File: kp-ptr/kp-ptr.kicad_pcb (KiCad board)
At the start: 4 copper layers, 31.6 x 104.6 mm, 169 parts, among them IC1 E22-900M22S, J1 ESP32_PROG_CON, J10 Conn_01x02, J11 Conn_01x02, J12 Conn_01x02, J13 Conn_01x02, J2 Conn_01x02, J3 Conn_01x02, J4 USB_C_Receptacle_USB2.0, J5 u.fl, J6 Conn_01x06_Male, J7 Conn_01x10_Male, J8 Conn_01x06_Male, J9 Conn_01x02_Male, Q1 NMOS_SOT23, Q2 DMC2025UFDB_v2, Q3 DMC2025UFDB_v2, Q4 DMC2025UFDB_v2, Q5 DMC2025UFDB_v2, U1 ESP32-S3FN8, U10 W25Q128JVS, U11 NL27WZU04DBVT1G, U2 MS560702BA03-50, U3 MMC5983MA, U4 H3LIS331, U5 L76-L, U6 NJG1156PCD, U7 LSM6DSO32, U9 USBLC6-2SC6, Y1 7M40000005-40MHz

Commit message: swiatelko w tunelu aby zmiescic wszystko
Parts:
- IC1, J4, J6, J7, J8, LS1, U5: moved to B.Cu
- J10, J12, J3: footprint TerminalBlock_Phoenix:TerminalBlock_Phoenix_MPT-0,5-2-2.54_1x02_P2.54mm_Horizontal -> TerminalBlock_TE-Connectivity:TerminalBlock_TE_282834-2_1x02_P2.54mm_Horizontal; moved to B.Cu
- J11, J13: footprint TerminalBlock_Phoenix:TerminalBlock_Phoenix_MPT-0,5-2-2.54_1x02_P2.54mm_Horizontal -> TerminalBlock_TE-Connectivity:TerminalBlock_TE_282834-2_1x02_P2.54mm_Horizontal
- J2: footprint Connector_JST:JST_GH_SM02B-GHS-TB_1x02-1MP_P1.25mm_Horizontal -> TerminalBlock_TE-Connectivity:TerminalBlock_TE_282834-2_1x02_P2.54mm_Horizontal; moved to B.Cu
- J9: footprint Connector_JST:JST_GH_BM02B-GHS-TBT_1x02-1MP_P1.25mm_Vertical -> TerminalBlock_TE-Connectivity:TerminalBlock_TE_282834-2_1x02_P2.54mm_Horizontal; moved to B.Cu
- moved C20 172.2 mm to (165.3, 49.3)
- moved C21 172.2 mm to (165.3, 48.3)
- moved R15 172.2 mm to (170.3, 47.3)
- moved U4 172.2 mm to (167.8, 48.8)
- moved C22 172.2 mm to (165.3, 50.3)
- moved C28 163.4 mm to (146.4, 37.3)
- moved C29 163.4 mm to (147.1, 37.3)
- moved C31 163.4 mm to (147.8, 37.3)
- moved R18 163.4 mm to (152.0, 39.3)
- moved U7 163.4 mm to (149.8, 38.2)
- moved R30 46.1 mm to (157.6, 40.8), turned to 0 degrees
- moved C39 28.7 mm to (163.6, 57.7)
- moved R26 28.7 mm to (165.6, 53.0)
- moved R27 28.7 mm to (172.0, 56.5)
- moved C40 28.7 mm to (162.6, 57.7)
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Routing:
- net VBUS: track 9.83 -> 0.00 mm
- net Net-(J4-PadA7): track 2.94 -> 0.00 mm
- net Net-(J4-PadA6): track 2.85 -> 0.00 mm
- net (no net): vias 0 -> 4
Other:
- board size 31.6 x 104.6 mm -> 31.6 x 101.5 mm

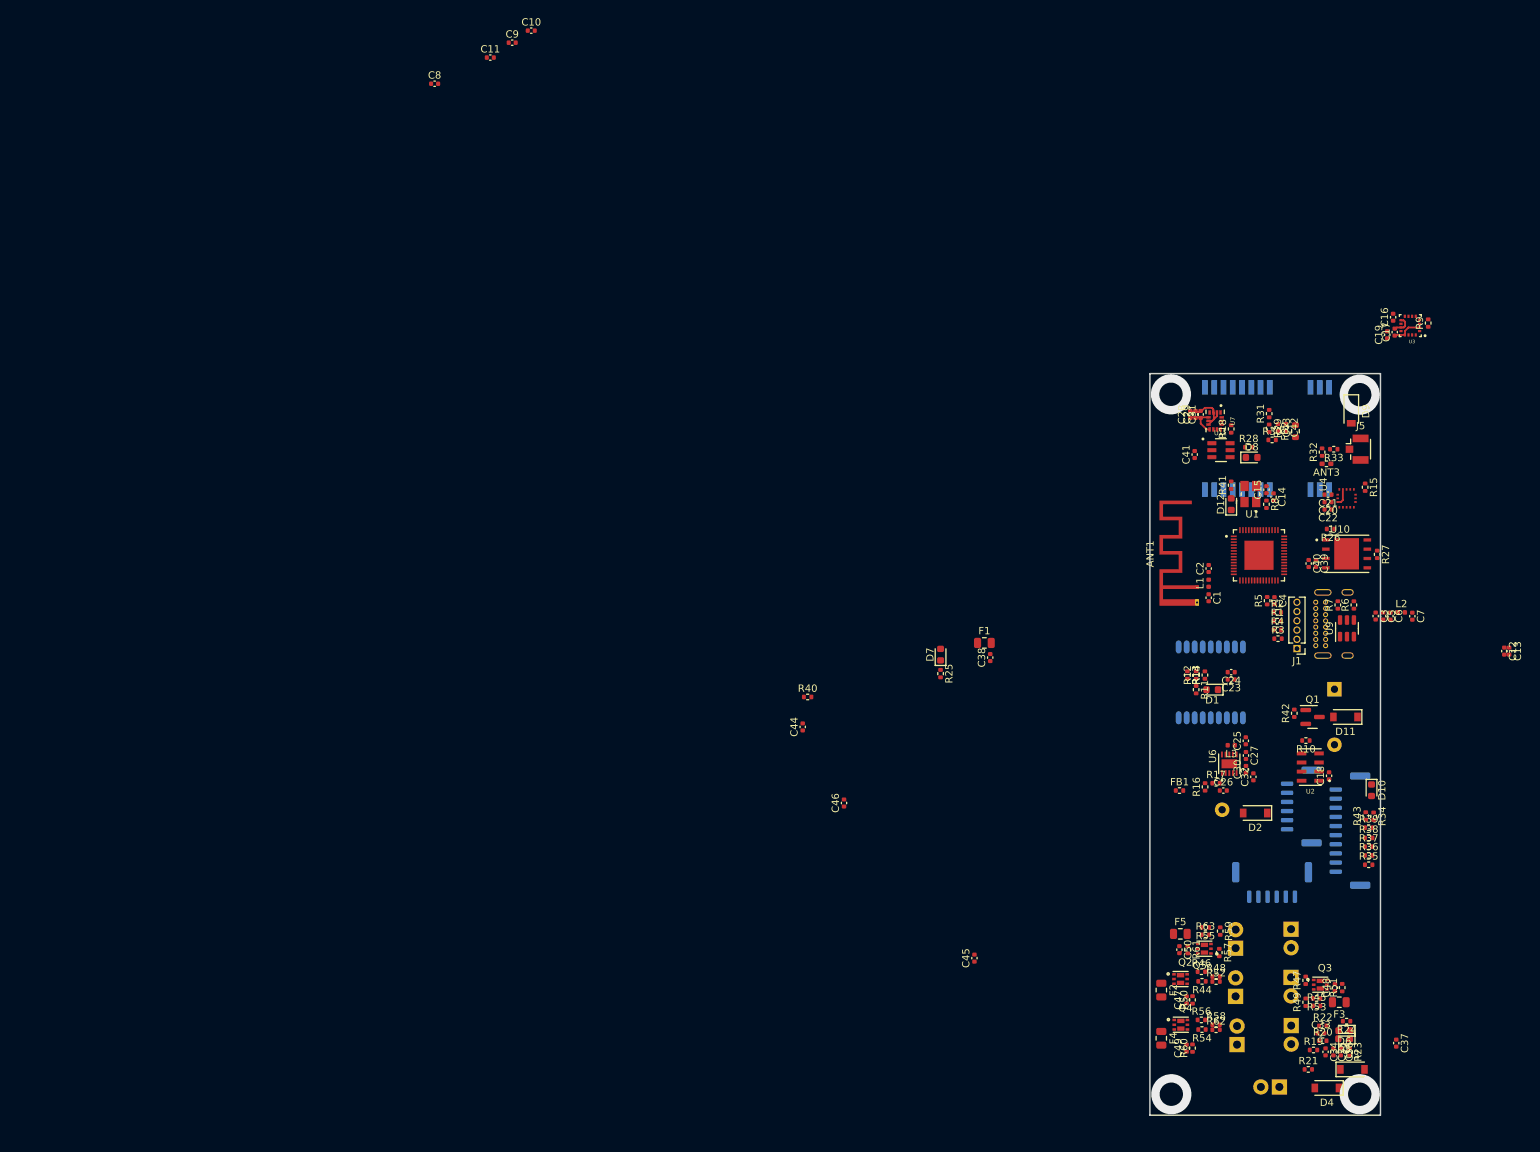
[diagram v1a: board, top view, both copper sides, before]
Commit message: chyba wszystkie footprinty
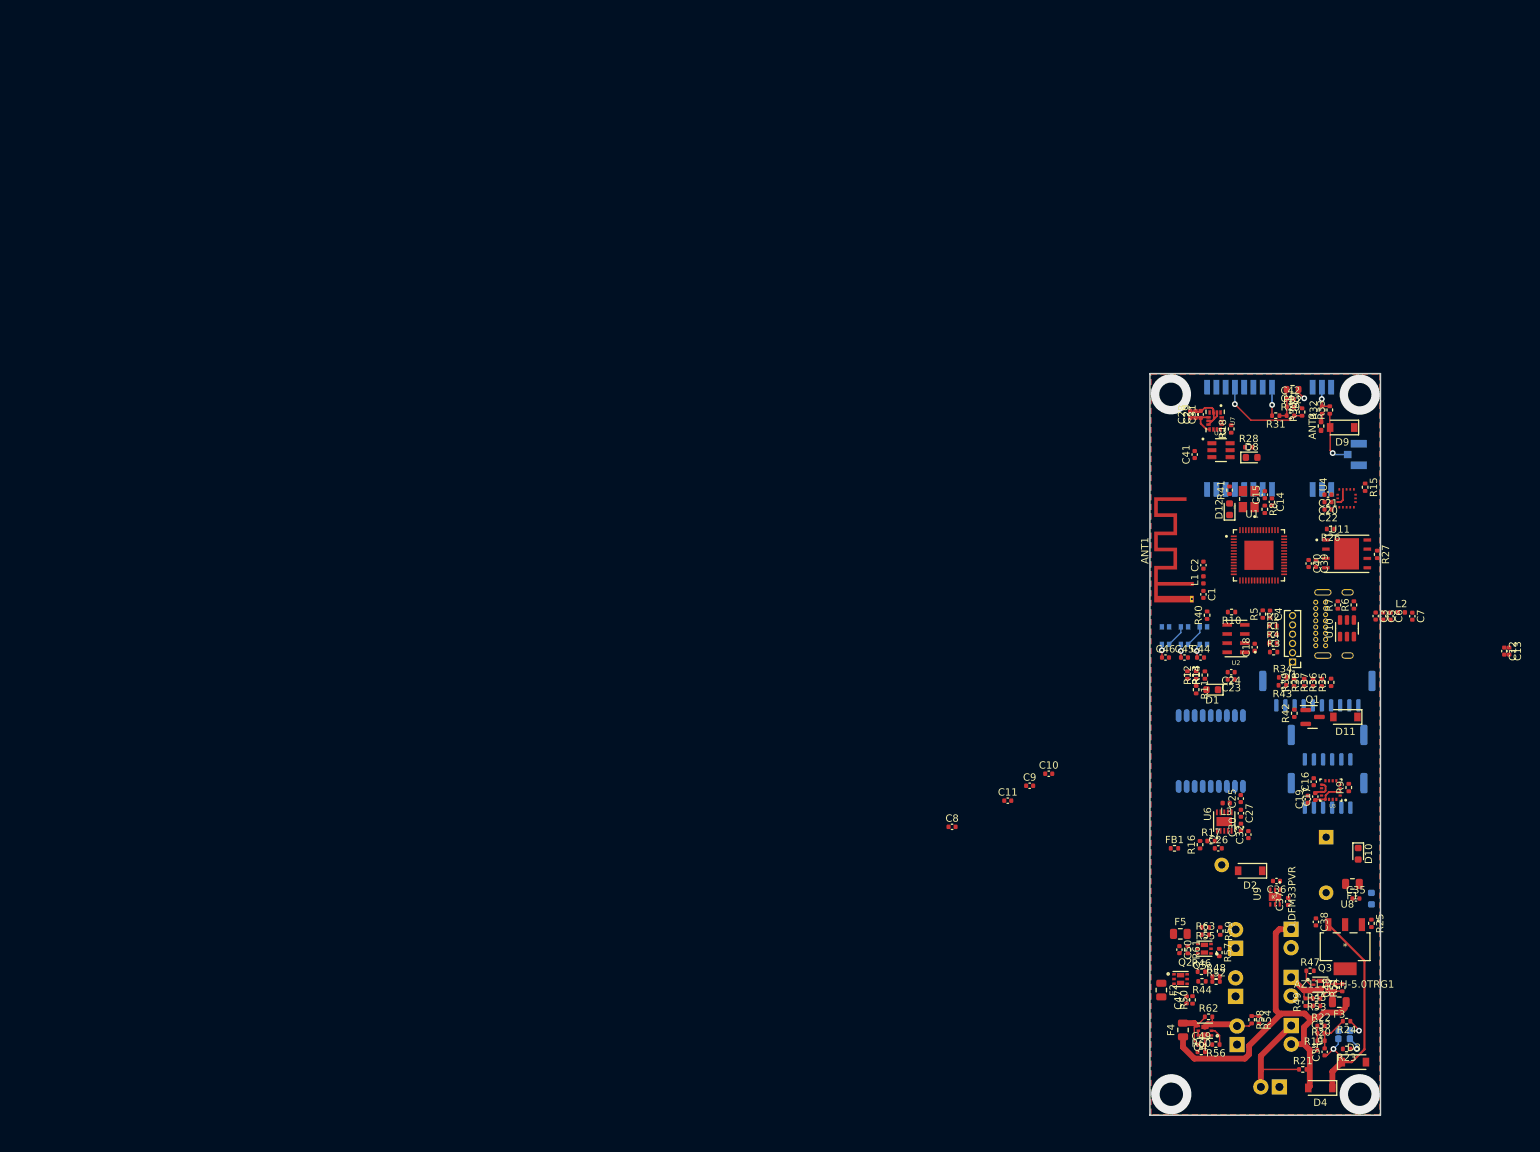
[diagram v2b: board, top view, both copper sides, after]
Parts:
- added D13: WS2812B-2020, KP-PTR_lib:WS2812B-2020, B.Cu at (148.2, 67.6)
- added D14: WS2812B-2020, KP-PTR_lib:WS2812B-2020, B.Cu at (145.6, 67.6)
- added D15: WS2812B-2020, KP-PTR_lib:WS2812B-2020, B.Cu at (143.0, 67.6)
- added U8: AZ1117CH-5.0TRG1, KP-PTR_lib:AZ1117CH-5.0TRG1, F.Cu at (167.6, 110.2)
- added U9: LDFM33PVR, KP-PTR_lib:LDFM33PVR, F.Cu at (158.0, 103.4)
- D5, D6, D7, J5: moved to B.Cu
- moved C10 124.0 mm to (127.0, 86.5)
- moved C11 124.0 mm to (121.4, 90.2)
- moved C8 124.0 mm to (113.8, 93.8)
- moved C9 124.0 mm to (124.4, 88.2)
- moved R25 68.2 mm to (171.2, 107.0)
- moved D7 67.8 mm to (171.2, 103.6)
- moved C19 64.5 mm to (162.5, 90.0)
- moved R9 64.5 mm to (168.1, 88.4)
- moved U3 64.5 mm to (165.6, 88.8)
- moved C16 64.5 mm to (163.3, 87.6)
- moved C17 64.5 mm to (163.5, 89.6)
- moved F1 60.2 mm to (168.6, 101.6), turned to 180 degrees
- moved C35 60.0 mm to (169.1, 103.6), turned to 0 degrees
- moved R40 55.8 mm to (148.7, 64.8), turned to 90 degrees
- moved C44 55.3 mm to (147.8, 70.6), turned to 0 degrees
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- renumbered C38 to C35, C37 to C36, C35 to C37, C36 to C38, U9 to U10, U10 to U11, U11 to U12
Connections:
- J12 pad 1: Net-(J12-Pad1) -> Earth
- J12 pad 2: Earth -> Net-(Q4-Pad3)
- Q4 pad 3: Net-(J12-Pad1) -> Net-(Q4-Pad3)
- R58 pad 2: Net-(J12-Pad1) -> Net-(Q4-Pad3)
- R62 pad 2: Net-(J12-Pad1) -> Net-(Q4-Pad3)
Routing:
- net VCC: track 0.00 -> 54.2 mm
- net VDD: track 0.00 -> 32.5 mm, vias 0 -> 1
- net +BATT: track 0.00 -> 15.4 mm
- net RF_RST: track 0.00 -> 12.7 mm, vias 0 -> 1
- net Net-(Q4-Pad3): track 0.00 -> 7.82 mm
- net Net-(D9-Pad2): track 0.00 -> 7.69 mm, vias 0 -> 1
- net +3V3: track 9.26 -> 16.4 mm, vias 0 -> 4
- net Net-(J11-Pad1): track 0.00 -> 7.15 mm
- net Net-(C49-Pad1): track 0.00 -> 6.60 mm
- net Earth: track 12.4 -> 18.0 mm
- net +3.3VP: track 0.00 -> 4.61 mm
- net Net-(C48-Pad1): track 0.00 -> 4.51 mm
- net Net-(C49-Pad2): track 0.00 -> 3.98 mm
- net SPI_CS_LORA: track 0.00 -> 3.92 mm, vias 0 -> 1
- net Net-(C48-Pad2): track 0.00 -> 3.75 mm
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- added copper zone on In2.Cu, net +3V3
- added copper zone on B.Cu, net Earth
- added copper zone on F.Cu, net Earth
- added copper zone on In1.Cu, net Earth

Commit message: PCB update
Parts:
- removed ANT1: PCB_antenna, RF_Antenna:Texas_SWRA117D_2.4GHz_Right
- removed ANT3: TBD, Resistor_SMD:R_0402_1005Metric_Pad0.72x0.64mm_HandSolder
- removed C27: DNP, Capacitor_SMD:C_0402_1005Metric
- removed R33: 0R, Resistor_SMD:R_0402_1005Metric
- C34: footprint Capacitor_SMD:C_0402_1005Metric -> Capacitor_SMD:CP_Elec_10x10; moved to B.Cu
- C44, C45, C46, D1, D10, D12, J1, R14: moved to B.Cu
- D2: footprint Diode_SMD:D_SOD-123 -> Diode_SMD:D_0402_1005Metric
- D9: footprint Diode_SMD:D_SOD-123 -> Diode_SMD:D_0402_1005Metric; moved to B.Cu
- J4: footprint Connector_USB:USB_C_Receptacle_GCT_USB4085 -> KP-PTR_lib:USB_C_213716
- J5: footprint Connector_Coaxial:U.FL_Hirose_U.FL-R-SMT-1_Vertical -> Connector_Coaxial:SMA_Amphenol_132289_EdgeMount
- R21: footprint Resistor_SMD:R_0402_1005Metric -> Resistor_SMD:R_1206_3216Metric
- R27: value 100k -> 10k
- R32: value DNP -> 10k
- U5: moved to F.Cu
- moved R32 51.3 mm to (163.3, 88.0), turned to 0 degrees
- moved C8 49.4 mm to (150.2, 60.5), turned to 90 degrees
- moved D3 48.1 mm to (166.7, 77.9), turned to 180 degrees
- moved C17 45.9 mm to (167.9, 43.9), turned to 0 degrees
- moved C11 45.4 mm to (153.0, 57.7), turned to 90 degrees
- moved R9 44.5 mm to (165.6, 43.9), turned to 0 degrees
- moved C19 44.2 mm to (169.3, 46.4)
- moved U3 42.6 mm to (167.0, 46.2), turned to -90 degrees
- moved C16 39.2 mm to (166.5, 48.6), turned to 180 degrees
- moved R40 38.2 mm to (185.4, 54.1), turned to 180 degrees
- moved C46 37.4 mm to (166.8, 41.7), turned to -90 degrees
- moved C9 37.3 mm to (149.4, 60.5), turned to 90 degrees
- moved C10 37.3 mm to (158.6, 66.8), turned to -45 degrees
- moved D15 36.9 mm to (169.3, 41.7), turned to 180 degrees
- moved R27 33.8 mm to (163.3, 89.2), turned to 0 degrees
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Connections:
- C30 pad 1: Net-(C30-Pad1) -> Net-(ANT2-Pad1)
- C30 pad 2: Net-(C27-Pad2) -> Net-(C25-Pad2)
- C32 pad 2: Net-(C30-Pad1) -> Net-(C32-Pad2)
- C38 pad 1: VDD -> VCC
- D8 pad 1: Net-(D8-Pad1) -> Net-(U12-Pad6)
- D9 pad 2: Net-(D9-Pad2) -> Net-(IC1-Pad21)
- J10 pad 1: Net-(J10-Pad1) -> Earth
- J10 pad 2: Earth -> Net-(J10-Pad2)
- J11 pad 1: Net-(J11-Pad1) -> Earth
- J11 pad 2: Earth -> Net-(J11-Pad2)
- J13 pad 1: Net-(J13-Pad1) -> Earth
- J13 pad 2: Earth -> Net-(J13-Pad2)
- J3 pad 1: +BATT -> VCC
- J3 pad 2: VCC -> +BATT
- J5 pad 1: Net-(D9-Pad2) -> Net-(IC1-Pad21)
- Q2 pad 3: Net-(J10-Pad1) -> Net-(J10-Pad2)
- Q3 pad 3: Net-(J11-Pad1) -> Net-(J11-Pad2)
- Q5 pad 3: Net-(J13-Pad1) -> Net-(J13-Pad2)
- R27 pad 1: +3V3 -> I2C_SCL
- R27 pad 2: SPI_CLK -> +3V3
- R32 pad 1: Net-(ANT3-Pad2) -> I2C_SDA
- R32 pad 2: Net-(IC1-Pad21) -> +3V3
- R48 pad 2: Net-(J10-Pad1) -> Net-(J10-Pad2)
- R49 pad 2: Net-(J11-Pad1) -> Net-(J11-Pad2)
- R52 pad 2: Net-(J10-Pad1) -> Net-(J10-Pad2)
- R53 pad 2: Net-(J11-Pad1) -> Net-(J11-Pad2)
- R59 pad 2: Net-(J13-Pad1) -> Net-(J13-Pad2)
- R63 pad 2: Net-(J13-Pad1) -> Net-(J13-Pad2)
- U10 pad 1: Net-(J4-PadA6) -> Net-(J4-PadA7)
- U10 pad 3: Net-(J4-PadA7) -> Net-(J4-PadA6)
- U10 pad 4: USB_DM -> USB_DP
- U10 pad 6: USB_DP -> USB_DM
- U12 pad 4: Net-(D8-Pad1) -> Net-(IC1-Pad6)
- U12 pad 6: Net-(IC1-Pad6) -> Net-(U12-Pad6)
- U6 pad 5: Net-(C30-Pad1) -> Net-(C32-Pad2)
- U8 pad 3: VDD -> VCC
- U8 pad 4: unconnected-(U8-Pad4) -> Net-(C35-Pad1)
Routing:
- net VCC: track 54.2 -> 0.00 mm
- net VDD: track 32.5 -> 0.00 mm, vias 1 -> 0
- net Earth: track 18.0 -> 0.02 mm
- net +3V3: track 16.4 -> 0.00 mm, vias 4 -> 0
- net +BATT: track 15.4 -> 0.00 mm
- net RF_RST: track 12.7 -> 0.00 mm, vias 1 -> 0
- net Net-(J12-Pad2): track 7.82 -> 0.00 mm
- net Net-(D9-Pad2): track 7.69 -> 0.00 mm, vias 1 -> 0
- net Net-(J11-Pad1): track 7.15 -> 0.00 mm
- net Net-(C49-Pad1): track 6.60 -> 0.00 mm
- net +3.3VP: track 4.61 -> 0.00 mm
- net Net-(C48-Pad1): track 4.51 -> 0.00 mm
- net Net-(C49-Pad2): track 3.98 -> 0.00 mm
- net SPI_CS_LORA: track 3.92 -> 0.00 mm, vias 1 -> 0
- net Net-(C48-Pad2): track 3.75 -> 0.00 mm
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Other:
- board size 31.6 x 101.5 mm -> 31.4 x 101.5 mm

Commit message: PCB update 2
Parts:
- moved C1 4.13 mm to (147.5, 62.1), turned to 90 degrees
- moved C4 2.40 mm to (150.3, 68.5)
- moved R5 2.15 mm to (150.3, 66.5)
- moved C6 2.04 mm to (148.8, 66.9), turned to 180 degrees
- moved L2 1.26 mm to (149.4, 65.5), turned to 45 degrees
- moved R8 1.15 mm to (150.2, 59.0), turned to 0 degrees
- moved C5 0.85 mm to (148.8, 67.7), turned to 180 degrees
- moved R41 0.78 mm to (151.7, 54.7), turned to -90 degrees
- moved L1 0.74 mm to (148.0, 63.6), turned to 0 degrees
- moved C17 0.69 mm to (167.3, 43.5), turned to 90 degrees
- moved C3 0.39 mm to (148.8, 68.5), turned to 180 degrees
- moved C11 0.31 mm to (153.1, 57.4)
- moved C7 0.18 mm to (150.1, 64.2)
- moved J8 0.09 mm to (163.2, 89.9)
- moved C13 0.05 mm to (161.0, 60.9), turned to 0 degrees
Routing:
- net SPI_MOSI: track 0.00 -> 63.8 mm, vias 0 -> 6
- net SPI_CLK: track 0.00 -> 59.8 mm, vias 0 -> 5
- net RF_RST: track 0.00 -> 49.7 mm, vias 0 -> 5
- net SPI_MISO: track 0.00 -> 49.3 mm, vias 0 -> 5
- net VCC: track 0.00 -> 40.2 mm, vias 0 -> 1
- net +3V3: track 0.00 -> 35.3 mm, vias 0 -> 11
- net BUZZER: track 0.00 -> 30.3 mm, vias 0 -> 2
- net VBUS: track 0.00 -> 25.2 mm, vias 0 -> 2
- net SPI_CS_MS5607: track 0.00 -> 23.5 mm
- net SPI_CS_MAG: track 0.00 -> 23.2 mm, vias 0 -> 4
- net RF_BUSY: track 0.00 -> 22.9 mm, vias 0 -> 3
- net Earth: track 0.02 -> 21.7 mm, vias 0 -> 23
- net SPI_CS_LORA: track 0.00 -> 20.6 mm, vias 0 -> 1
- net BOOT_PIN: track 0.00 -> 19.2 mm, vias 0 -> 2
- net IGN3_DET: track 0.00 -> 18.2 mm
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
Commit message: SCH&PCB update
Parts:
- added AE1: Antenna_Chip, KP-PTR_lib:AMCA31-2R450G-S1F-T3, F.Cu at (142.5, 65.9)
- C44, C45, C46: moved to F.Cu
- D8: moved to B.Cu
- moved D12 22.4 mm to (149.9, 33.8), turned to -90 degrees
- moved R40 21.8 mm to (165.9, 63.9)
- moved R41 18.4 mm to (149.1, 36.5)
- moved C40 8.30 mm to (169.5, 56.8), turned to 180 degrees
- moved C39 7.02 mm to (169.5, 57.7), turned to 180 degrees
- moved U10 6.71 mm to (168.2, 71.2), turned to 0 degrees
- moved D11 6.07 mm to (158.2, 80.0), turned to 135 degrees
- moved J2 3.89 mm to (160.0, 125.8)
- moved R34 3.35 mm to (166.1, 83.3), turned to 180 degrees
- moved C44 2.68 mm to (167.7, 56.5), turned to 90 degrees
- moved R38 2.61 mm to (166.1, 85.5), turned to 180 degrees
- moved R39 2.61 mm to (166.1, 84.3), turned to 180 degrees
- moved R37 2.61 mm to (166.1, 86.7), turned to 180 degrees
- moved R35 2.61 mm to (166.1, 89.3), turned to 180 degrees
- moved R36 2.61 mm to (166.1, 88.0), turned to 180 degrees
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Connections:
- net Net-(C47-Pad1) renamed IGN1_PWR
- net Net-(C48-Pad1) renamed IGN3_PWR
- net Net-(C49-Pad1) renamed IGN2_PWR
- net Net-(C50-Pad1) renamed IGN4_PWR
- J2 pad 1: Earth -> +BATT
- J2 pad 2: +BATT -> Earth
- U1 pad 10: GPIO5 -> IGN1_DET
- U1 pad 11: GPIO6 -> IGN2_DET
- U1 pad 12: GPIO7 -> IGN3_DET
- U1 pad 13: GPIO8 -> VBAT_MEAS
- U1 pad 14: GPIO9 -> IGN3_EN
- U1 pad 15: GPIO10 -> IGN2_EN
- U1 pad 16: GPIO11 -> IGN1_EN
- U1 pad 17: GPIO12 -> IGN4_EN
- U1 pad 18: GPIO13 -> UART1_OUT
- U1 pad 19: GPIO14 -> UART1_IN
- U1 pad 21: GPIO15 -> I2C_SDA
- U1 pad 22: GPIO16 -> I2C_SCL
- U1 pad 23: GPIO17 -> SERVO_1
- U1 pad 24: GPIO18 -> SERVO_2
- U1 pad 27: GPIO21 -> SERVO_3
- U1 pad 28: GPIO26 -> SERVO_4
- U1 pad 36: GPIO48 -> SERVO_EN
- U1 pad 37: GPIO47 -> LED1
- U1 pad 38: GPIO33 -> SPI_CS_FLASH
- U1 pad 39: GPIO34 -> SPI_CS_MAG
- U1 pad 40: GPIO35 -> SPI_CS_LSM
- U1 pad 41: GPIO36 -> SPI_CS_LIS
- U1 pad 42: GPIO37 -> RF_BUSY
- U1 pad 43: GPIO38 -> SPI_MISO
- U1 pad 44: GPIO39 -> SPI_MOSI
- U1 pad 45: GPIO40 -> SPI_CLK
- U1 pad 47: GPIO41 -> SPI_CS_MS5607
- U1 pad 48: GPIO42 -> SPI_CS_LORA
- U1 pad 6: GPIO1 -> GPS_IN
- U1 pad 7: GPIO2 -> GPS_OUT
- U1 pad 9: GPIO4 -> IGN4_DET
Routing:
- net IGN3_EN: track 1.08 -> 58.9 mm, vias 0 -> 2
- net IGN2_EN: track 0.00 -> 55.1 mm, vias 0 -> 4
- net VDD: track 0.00 -> 52.3 mm, vias 0 -> 7
- net IGN1_EN: track 0.00 -> 51.3 mm, vias 0 -> 4
- net VBAT_MEAS: track 0.00 -> 50.9 mm
- net Earth: track 21.7 -> 71.6 mm, vias 23 -> 149
- net IGN2_DET: track 0.00 -> 48.2 mm
- net IGN4_EN: track 0.00 -> 44.0 mm, vias 0 -> 2
- net IGN1_DET: track 0.00 -> 42.5 mm
- net +5V: track 0.00 -> 41.2 mm, vias 0 -> 3
- net SERVO_EN: track 1.12 -> 38.4 mm, vias 0 -> 4
- net IGN3_DET: track 18.2 -> 54.4 mm
- net IGN4_DET: track 0.00 -> 35.8 mm
- net SERVO_4: track 0.00 -> 30.1 mm, vias 0 -> 2
- net SERVO_3: track 0.00 -> 30.0 mm, vias 0 -> 2
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- added copper zone on In2.Cu, net +3.3VADC
- added copper zone on In2.Cu, net +3.3VP
- added copper zone on In2.Cu, net +BATT
- added copper zone on In2.Cu, net IGN1_PWR
- added copper zone on In2.Cu, net IGN2_PWR
- added copper zone on In2.Cu, net IGN3_PWR
- added copper zone on In2.Cu, net IGN4_PWR
- added copper zone on In2.Cu, net VCC
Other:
- board size 31.4 x 101.5 mm -> 31 x 101 mm
- board text added: "+"
- board text added: "3V3"
- board text added: "5V"
- board text added: "ARM"
- board text added: "BAT max 13V"
- board text added: "BOOT"
- board text added: "EN"
- board text added: "GND"
- board text added: "IGN1"
- board text added: "IGN2"
- board text added: "IGN3"
- board text added: "IGN4"
- board text added: "NC"
- board text added: "READY"
- board text added: "RX"
- board text added: "STAT"
- board text added: "SWITCH"
- board text added: "TX"
- board text added: "VIN"
- board text added: "}Vout"
